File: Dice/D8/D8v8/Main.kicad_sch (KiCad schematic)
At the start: 29 parts, among them J1 Conn_01x14, J2 Conn_01x04, J4 DNP, U1 NRF52810-CAAA-R, U2 SC7A20HTR, U5 BL24C02F-NTRC, U8 SL1605, Y1 32MHz 40ppm

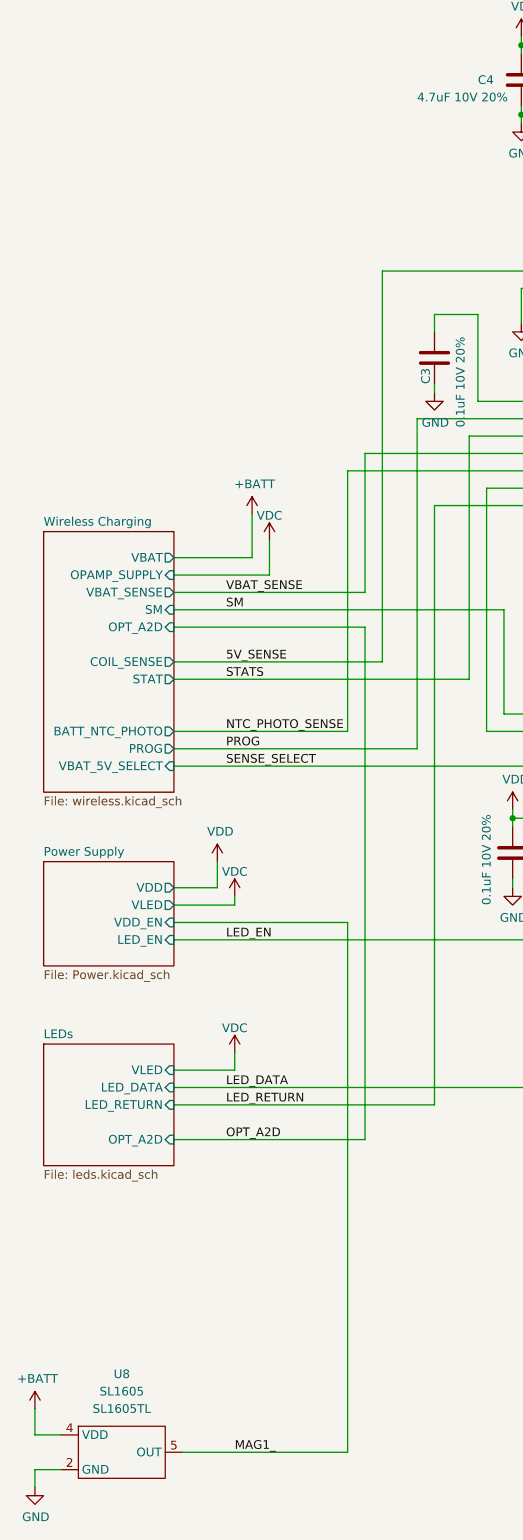
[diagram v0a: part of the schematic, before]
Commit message: Updated schematic Titles in D20V17 and likes, added 12mm D6 and Charging Jig
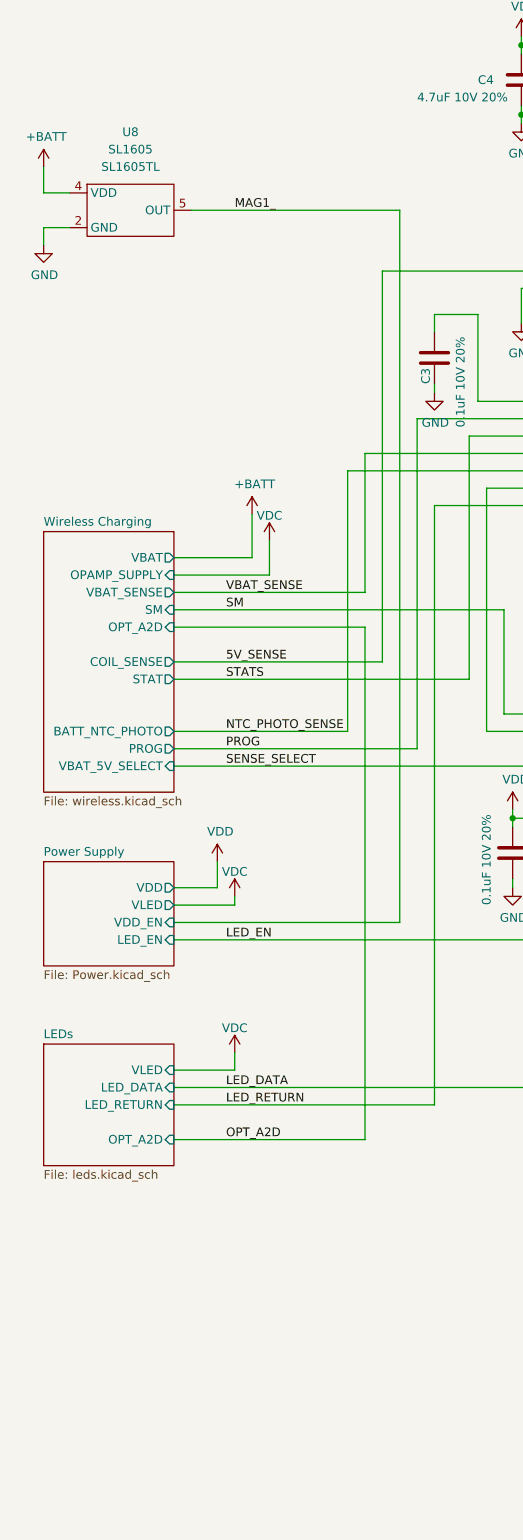
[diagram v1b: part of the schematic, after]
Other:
- title: Pixels D20 Schematic, Main -> Pixels D8V8 Schematic, Main
- moved on the sheet: U8
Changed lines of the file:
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@@
 	(paper "A4")
 	(title_block
-		(title "Pixels D20 Schematic, Main")
-		(date "2022-08-26")
+		(title "Pixels D8V8 Schematic, Main")
+		(date "2025-10-10")
 		(rev "13")
 		(company "Systemic Games, LLC")
@@
 	(wire
 		(pts
-			(xy 39.37 149.86) (xy 64.77 149.86)
+			(xy 39.37 149.86) (xy 72.39 149.86)
 		)
 		(stroke
@@
 	(wire
 		(pts
-			(xy 40.64 227.33) (xy 64.77 227.33)
+			(xy 41.91 45.72) (xy 72.39 45.72)
 		)
 		(stroke
@@
 	(wire
 		(pts
-			(xy 19.05 220.98) (xy 19.05 224.79)
+			(xy 20.32 39.37) (xy 20.32 43.18)
 		)
 		(stroke
@@
 	(wire
 		(pts
-			(xy 64.77 149.86) (xy 64.77 227.33)
+			(xy 72.39 149.86) (xy 72.39 45.72)
 		)
 		(stroke
@@
 	(wire
 		(pts
-			(xy 22.86 229.87) (xy 19.05 229.87)
+			(xy 24.13 48.26) (xy 20.32 48.26)
 		)
 		(stroke
@@
 	(wire
 		(pts
-			(xy 19.05 229.87) (xy 19.05 232.41)
+			(xy 20.32 48.26) (xy 20.32 50.8)
 		)
 		(stroke
@@
 	(wire
 		(pts
-			(xy 19.05 224.79) (xy 22.86 224.79)
+			(xy 20.32 43.18) (xy 24.13 43.18)
 		)
 		(stroke
@@
 	)
 	(label "MAG1_"
-		(at 48.26 227.33 0)
+		(at 48.26 45.72 0)
 		(effects
 			(font
@@
 	(symbol
 		(lib_id "power:GND")
-		(at 19.05 232.41 0)
+		(at 20.32 50.8 0)
 		(unit 1)
 		(exclude_from_sim no)
@@
 		(dnp no)
 		(property "Reference" "#PWR045"
-			(at 19.05 238.76 0)
+			(at 20.32 57.15 0)
 			(effects
 				(font
@@
 		)
 		(property "Value" "GND"
-			(at 19.177 236.8042 0)
+			(at 20.447 55.1942 0)
 			(effects
 				(font
@@
 		)
 		(property "Footprint" ""
-			(at 19.05 232.41 0)
+			(at 20.32 50.8 0)
 			(effects
 				(font
@@
 		)
 		(property "Datasheet" ""
-			(at 19.05 232.41 0)
+			(at 20.32 50.8 0)
 			(effects
 				(font
@@
 		)
 		(property "Description" ""
-			(at 19.05 232.41 0)
+			(at 20.32 50.8 0)
 			(effects
 				(font
@@
 	(symbol
 		(lib_id "power:+BATT")
-		(at 19.05 220.98 0)
+		(at 20.32 39.37 0)
 		(unit 1)
 		(exclude_from_sim no)
@@
 		(dnp no)
 		(property "Reference" "#PWR017"
-			(at 19.05 224.79 0)
+			(at 20.32 43.18 0)
 			(effects
 				(font
@@
 		)
 		(property "Value" "+BATT"
-			(at 19.431 216.5858 0)
+			(at 20.701 34.9758 0)
 			(effects
 				(font
@@
 		)
 		(property "Footprint" ""
-			(at 19.05 220.98 0)
+			(at 20.32 39.37 0)
 			(effects
 				(font
@@
 		)
 		(property "Datasheet" ""
-			(at 19.05 220.98 0)
+			(at 20.32 39.37 0)
 			(effects
 				(font
@@
 		)
 		(property "Description" ""
-			(at 19.05 220.98 0)
+			(at 20.32 39.37 0)
 			(effects
 				(font
@@
 	(symbol
 		(lib_id "Pixels-dice:SL1605")
-		(at 31.75 227.33 0)
+		(at 33.02 45.72 0)
 		(unit 1)
 		(exclude_from_sim no)
@@
 		(fields_autoplaced yes)
 		(property "Reference" "U8"
-			(at 31.75 215.9 0)
+			(at 33.02 34.29 0)
 			(effects
 				(font
@@
 		)
 		(property "Value" "SL1605"
-			(at 31.75 218.44 0)
+			(at 33.02 36.83 0)
 			(effects
 				(font
@@
 		)
 		(property "Footprint" "Package_TO_SOT_SMD:SOT-553"
-			(at 31.75 227.33 0)
+			(at 33.02 45.72 0)
 			(effects
 				(font
@@
 		)
 		(property "Datasheet" ""
-			(at 31.75 227.33 0)
+			(at 33.02 45.72 0)
 			(effects
 				(font
@@
 		)
 		(property "Description" ""
-			(at 31.75 227.33 0)
+			(at 33.02 45.72 0)
 			(effects
 				(font
@@
 		)
 		(property "Manufacturer" "Slkor(SLKORMICRO Elec.)"
-			(at 31.75 227.33 0)
+			(at 33.02 45.72 0)
 			(effects
 				(font
@@
 		)
 		(property "Part Number" "SL1605TL"
-			(at 31.75 220.98 0)
+			(at 33.02 39.37 0)
 			(effects
 				(font
@@
 		)
 		(property "LCSC Part #" "C2826474"
-			(at 31.75 227.33 0)
+			(at 33.02 45.72 0)
 			(effects
 				(font
